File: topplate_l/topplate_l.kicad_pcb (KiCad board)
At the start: 2 copper layers, 133.3 x 104.8 mm, 28 parts, among them SW1 SW_PUSH, SW10 SW_PUSH, SW11 SW_PUSH, SW12 SW_PUSH, SW13 SW_PUSH, SW14 SW_PUSH, SW15 SW_PUSH, SW16 SW_PUSH, SW17 SW_PUSH, SW18 SW_PUSH, SW19 SW_PUSH, SW2 SW_PUSH, SW20 SW_PUSH, SW21 SW_PUSH, SW22 SW_PUSH, SW3 SW_PUSH, SW4 SW_PUSH, SW5 SW_PUSH, SW6 SW_PUSH, SW7 SW_PUSH, SW8 SW_PUSH, SW9 SW_PUSH

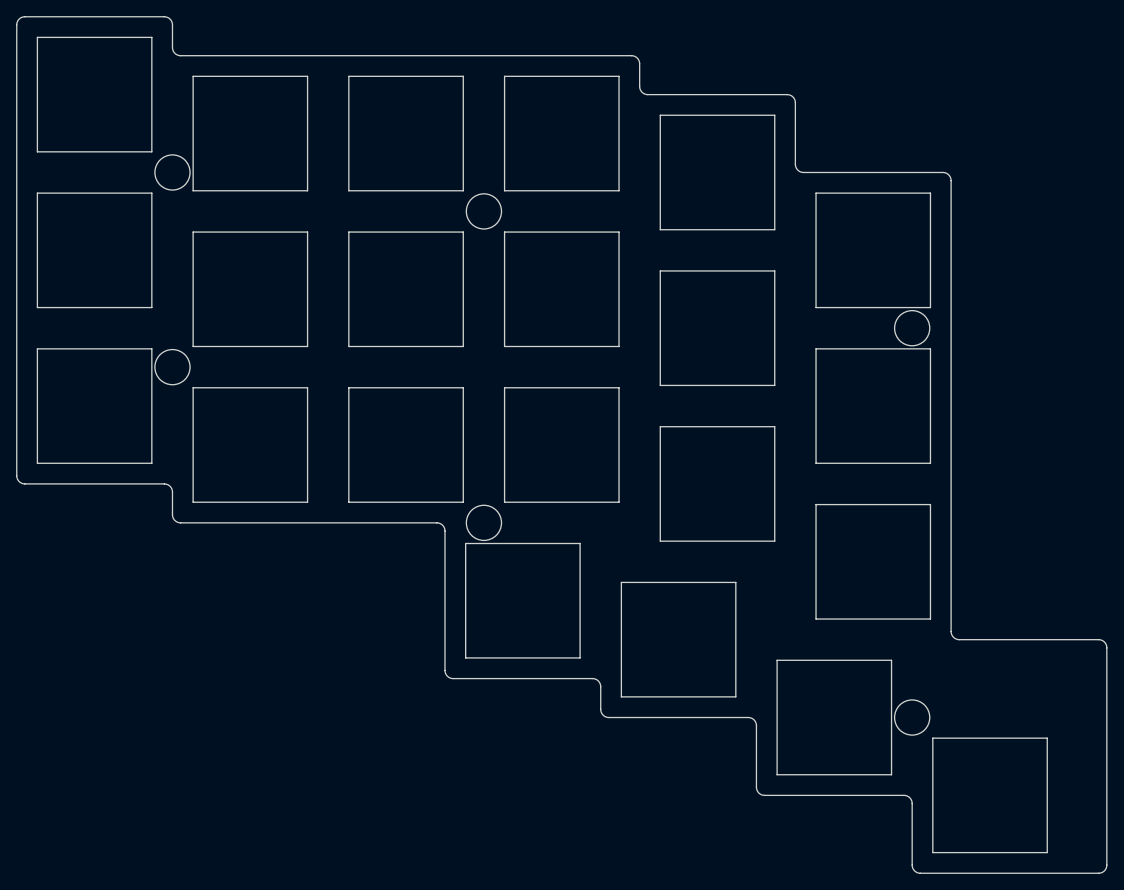
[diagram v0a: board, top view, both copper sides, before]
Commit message: added gnd mask
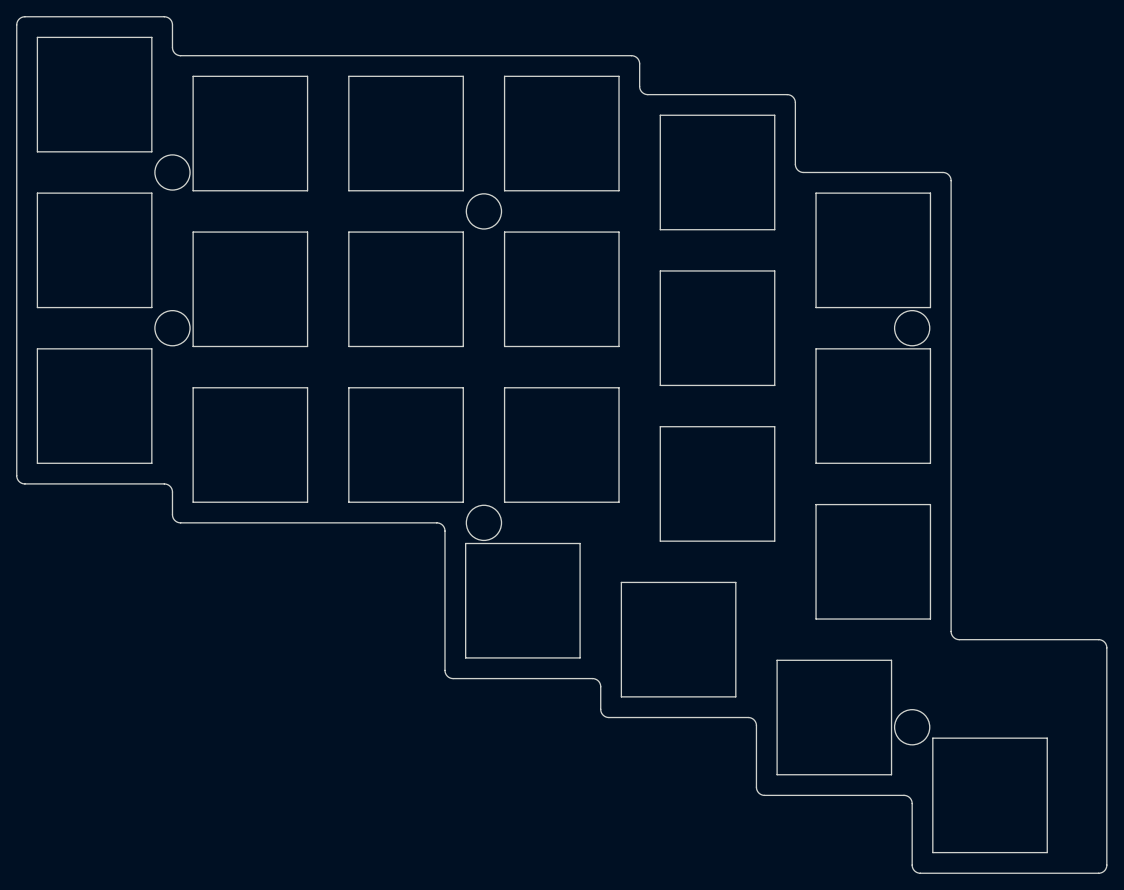
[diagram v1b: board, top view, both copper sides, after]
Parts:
- moved Ref** 4.76 mm to (38.1, 59.5)
- moved Ref** 1.19 mm to (128.6, 108.3)
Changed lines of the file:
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@@
   )
   (footprint "kbd:M2_HOLE_v2" (layer "F.Cu")
-    (at 38.1 64.29375)
+    (at 38.1 59.53125)
     (descr "Mounting Hole 2.2mm, no annular, M2")
     (tags "mounting hole 2.2mm no annular m2")
@@
   )
   (footprint "kbd:M2_HOLE_v2" (layer "F.Cu")
-    (at 128.5875 107.15625)
+    (at 128.5875 108.346875)
     (descr "Mounting Hole 2.2mm, no annular, M2")
     (tags "mounting hole 2.2mm no annular m2")

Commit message: fixed for order
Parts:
- Ref** (x6): footprint kbd:M2_HOLE_v2 -> kbd:M2_Hole_TH
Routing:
- added copper zone on F.Cu, net (none)
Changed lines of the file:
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@@
       (stroke (width 0.15) (type solid)) (layer "F.Fab"))
   )
-  (footprint "kbd:M2_HOLE_v2" (layer "F.Cu")
+  (footprint "kbd:M2_Hole_TH" (layer "F.Cu")
     (at 76.2 45.24375)
-    (descr "Mounting Hole 2.2mm, no annular, M2")
-    (tags "mounting hole 2.2mm no annular m2")
-    (attr exclude_from_pos_files exclude_from_bom)
-    (fp_text reference "Ref**" (at -0.95 -0.55) (layer "F.Fab") hide
-        (effects (font (size 1 1) (thickness 0.15)))
-    )
-    (fp_text value "Val**" (at 0 0.55) (layer "F.Fab") hide
-        (effects (font (size 1 1) (thickness 0.15)))
-    )
-    (pad "" np_thru_hole circle (at 0 0) (size 4.3 4.3) (drill 4.3) (layers "*.Cu" "*.Mask"))
-  )
-  (footprint "kbd:M2_HOLE_v2" (layer "F.Cu")
+    (attr through_hole)
+    (fp_text reference "Ref**" (at 0 0.5) (layer "F.SilkS")
+        (effects (font (size 1 1) (thickness 0.15)))
+    )
+    (fp_text value "Val**" (at 0 -0.5) (layer "F.Fab")
+        (effects (font (size 1 1) (thickness 0.15)))
+    )
+    (pad "" thru_hole circle (at 0 0) (size 4.2 4.2) (drill 2.3) (layers "*.Cu" "*.Mask"))
+  )
+  (footprint "kbd:M2_Hole_TH" (layer "F.Cu")
     (at 128.5875 59.53125)
-    (descr "Mounting Hole 2.2mm, no annular, M2")
-    (tags "mounting hole 2.2mm no annular m2")
-    (attr exclude_from_pos_files exclude_from_bom)
-    (fp_text reference "Ref**" (at -0.95 -0.55) (layer "F.Fab") hide
-        (effects (font (size 1 1) (thickness 0.15)))
-    )
-    (fp_text value "Val**" (at 0 0.55) (layer "F.Fab") hide
-        (effects (font (size 1 1) (thickness 0.15)))
-    )
-    (pad "" np_thru_hole circle (at 0 0) (size 4.3 4.3) (drill 4.3) (layers "*.Cu" "*.Mask"))
+    (attr through_hole)
+    (fp_text reference "Ref**" (at 0 0.5) (layer "F.SilkS")
+        (effects (font (size 1 1) (thickness 0.15)))
+    )
+    (fp_text value "Val**" (at 0 -0.5) (layer "F.Fab")
+        (effects (font (size 1 1) (thickness 0.15)))
+    )
+    (pad "" thru_hole circle (at 0 0) (size 4.2 4.2) (drill 2.3) (layers "*.Cu" "*.Mask"))
   )
   (footprint "kbd:SW_Hole" (layer "F.Cu")
@@
       (stroke (width 0.15) (type solid)) (layer "F.Fab"))
   )
-  (footprint "kbd:M2_HOLE_v2" (layer "F.Cu")
+  (footprint "kbd:M2_Hole_TH" (layer "F.Cu")
     (at 38.1 59.53125)
-    (descr "Mounting Hole 2.2mm, no annular, M2")
-    (tags "mounting hole 2.2mm no annular m2")
-    (attr exclude_from_pos_files exclude_from_bom)
-    (fp_text reference "Ref**" (at -0.95 -0.55) (layer "F.Fab") hide
-        (effects (font (size 1 1) (thickness 0.15)))
-    )
-    (fp_text value "Val**" (at 0 0.55) (layer "F.Fab") hide
-        (effects (font (size 1 1) (thickness 0.15)))
-    )
-    (pad "" np_thru_hole circle (at 0 0) (size 4.3 4.3) (drill 4.3) (layers "*.Cu" "*.Mask"))
+    (attr through_hole)
+    (fp_text reference "Ref**" (at 0 0.5) (layer "F.SilkS")
+        (effects (font (size 1 1) (thickness 0.15)))
+    )
+    (fp_text value "Val**" (at 0 -0.5) (layer "F.Fab")
+        (effects (font (size 1 1) (thickness 0.15)))
+    )
+    (pad "" thru_hole circle (at 0 0) (size 4.2 4.2) (drill 2.3) (layers "*.Cu" "*.Mask"))
   )
   (footprint "kbd:SW_Hole" (layer "F.Cu")
@@
       (stroke (width 0.15) (type solid)) (layer "F.Fab"))
   )
-  (footprint "kbd:M2_HOLE_v2" (layer "F.Cu")
+  (footprint "kbd:M2_Hole_TH" (layer "F.Cu")
     (at 38.1 40.48125)
-    (descr "Mounting Hole 2.2mm, no annular, M2")
-    (tags "mounting hole 2.2mm no annular m2")
-    (attr exclude_from_pos_files exclude_from_bom)
-    (fp_text reference "Ref**" (at -0.95 -0.55) (layer "F.Fab") hide
-        (effects (font (size 1 1) (thickness 0.15)))
-    )
-    (fp_text value "Val**" (at 0 0.55) (layer "F.Fab") hide
-        (effects (font (size 1 1) (thickness 0.15)))
-    )
-    (pad "" np_thru_hole circle (at 0 0) (size 4.3 4.3) (drill 4.3) (layers "*.Cu" "*.Mask"))
-  )
-  (footprint "kbd:M2_HOLE_v2" (layer "F.Cu")
+    (attr through_hole)
+    (fp_text reference "Ref**" (at 0 0.5) (layer "F.SilkS")
+        (effects (font (size 1 1) (thickness 0.15)))
+    )
+    (fp_text value "Val**" (at 0 -0.5) (layer "F.Fab")
+        (effects (font (size 1 1) (thickness 0.15)))
+    )
+    (pad "" thru_hole circle (at 0 0) (size 4.2 4.2) (drill 2.3) (layers "*.Cu" "*.Mask"))
+  )
+  (footprint "kbd:M2_Hole_TH" (layer "F.Cu")
     (at 128.5875 108.346875)
-    (descr "Mounting Hole 2.2mm, no annular, M2")
-    (tags "mounting hole 2.2mm no annular m2")
-    (attr exclude_from_pos_files exclude_from_bom)
-    (fp_text reference "Ref**" (at -0.95 -0.55) (layer "F.Fab") hide
-        (effects (font (size 1 1) (thickness 0.15)))
-    )
-    (fp_text value "Val**" (at 0 0.55) (layer "F.Fab") hide
-        (effects (font (size 1 1) (thickness 0.15)))
-    )
-    (pad "" np_thru_hole circle (at 0 0) (size 4.3 4.3) (drill 4.3) (layers "*.Cu" "*.Mask"))
+    (attr through_hole)
+    (fp_text reference "Ref**" (at 0 0.5) (layer "F.SilkS")
+        (effects (font (size 1 1) (thickness 0.15)))
+    )
+    (fp_text value "Val**" (at 0 -0.5) (layer "F.Fab")
+        (effects (font (size 1 1) (thickness 0.15)))
+    )
+    (pad "" thru_hole circle (at 0 0) (size 4.2 4.2) (drill 2.3) (layers "*.Cu" "*.Mask"))
   )
   (footprint "kbd:SW_Hole" (layer "F.Cu")
@@
       (stroke (width 0.15) (type solid)) (layer "F.Fab"))
   )
-  (footprint "kbd:M2_HOLE_v2" (layer "F.Cu")
+  (footprint "kbd:M2_Hole_TH" (layer "F.Cu")
     (at 76.2 83.34375)
-    (descr "Mounting Hole 2.2mm, no annular, M2")
-    (tags "mounting hole 2.2mm no annular m2")
-    (attr exclude_from_pos_files exclude_from_bom)
-    (fp_text reference "Ref**" (at -0.95 -0.55) (layer "F.Fab") hide
-        (effects (font (size 1 1) (thickness 0.15)))
-    )
-    (fp_text value "Val**" (at 0 0.55) (layer "F.Fab") hide
-        (effects (font (size 1 1) (thickness 0.15)))
-    )
-    (pad "" np_thru_hole circle (at 0 0) (size 4.3 4.3) (drill 4.3) (layers "*.Cu" "*.Mask"))
+    (attr through_hole)
+    (fp_text reference "Ref**" (at 0 0.5) (layer "F.SilkS")
+        (effects (font (size 1 1) (thickness 0.15)))
+    )
+    (fp_text value "Val**" (at 0 -0.5) (layer "F.Fab")
+        (effects (font (size 1 1) (thickness 0.15)))
+    )
+    (pad "" thru_hole circle (at 0 0) (size 4.2 4.2) (drill 2.3) (layers "*.Cu" "*.Mask"))
   )
   (footprint "kbd:SW_Hole" (layer "F.Cu")
@@
   (gr_arc (start 132.35 40.48125) (mid 133.057107 40.774143) (end 133.35 41.48125)
     (stroke (width 0.1) (type default)) (layer "Edge.Cuts"))
+  (zone (net 0) (net_name "") (layer "F.Cu") (hatch edge 0.5)
+    (connect_pads (clearance 1))
+    (min_thickness 0.25) (filled_areas_thickness no)
+    (fill yes (thermal_gap 0.5) (thermal_bridge_width 0.5) (island_removal_mode 1) (island_area_min 10))
+    (polygon
+      (pts
+        (xy 133.35 40.48125)
+        (xy 114.3 40.48125)
+        (xy 114.3 30.95625)
+        (xy 95.25 30.95625)
+        (xy 95.25 26.19375)
+        (xy 38.1 26.19375)
+        (xy 38.1 21.43125)
+        (xy 19.05 21.43125)
+        (xy 19.05 78.58125)
+        (xy 38.1 78.58125)
+        (xy 38.1 83.34375)
+        (xy 71.4375 83.34375)
+        (xy 71.4375 102.39375)
+        (xy 90.4875 102.39375)
+        (xy 90.4875 107.15625)
+        (xy 109.5375 107.15625)
+        (xy 109.5375 116.68125)
+        (xy 128.5875 116.68125)
+        (xy 128.5875 126.20625)
+        (xy 152.4 126.20625)
+        (xy 152.4 97.63125)
+        (xy 133.35 97.63125)
+      )
+    )
+  )
   (group "" (id b9ec9487-7741-4b36-bab2-a6f5571cd5b5)
     (members

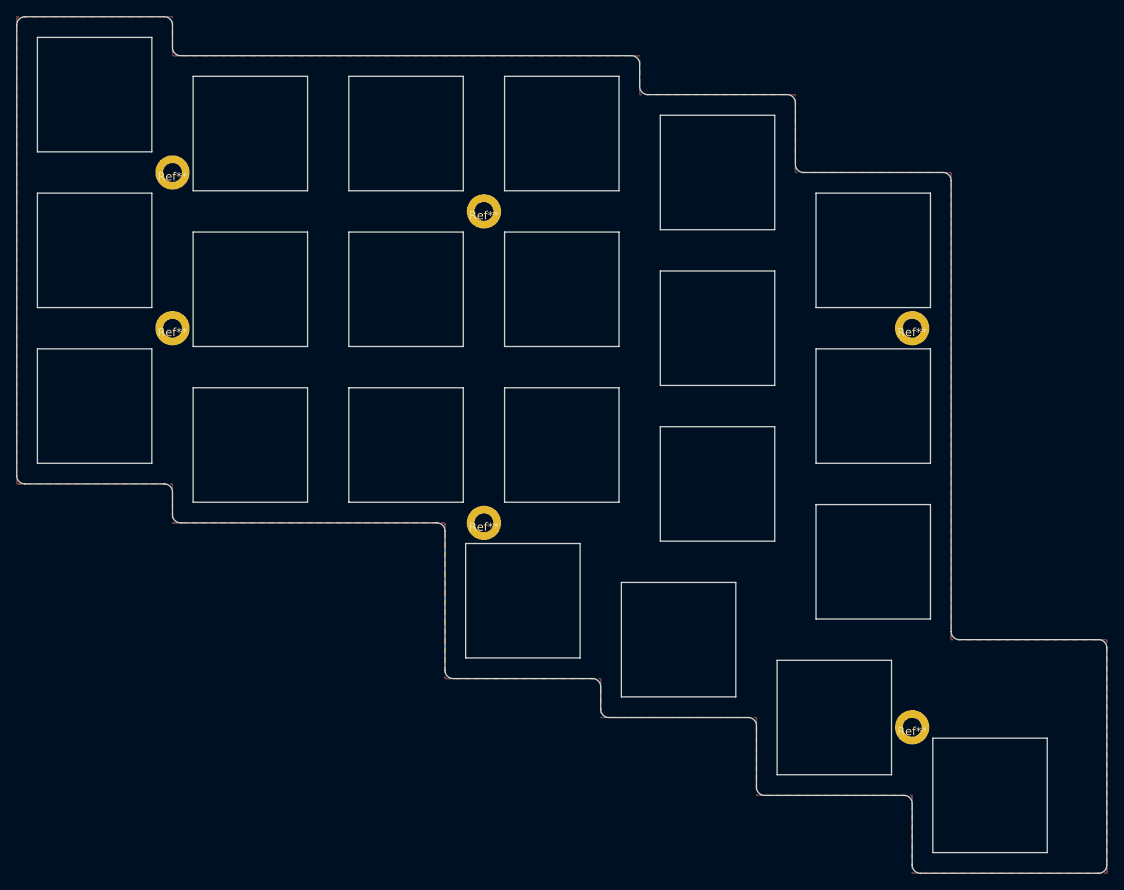
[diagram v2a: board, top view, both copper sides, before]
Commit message: fixed #6
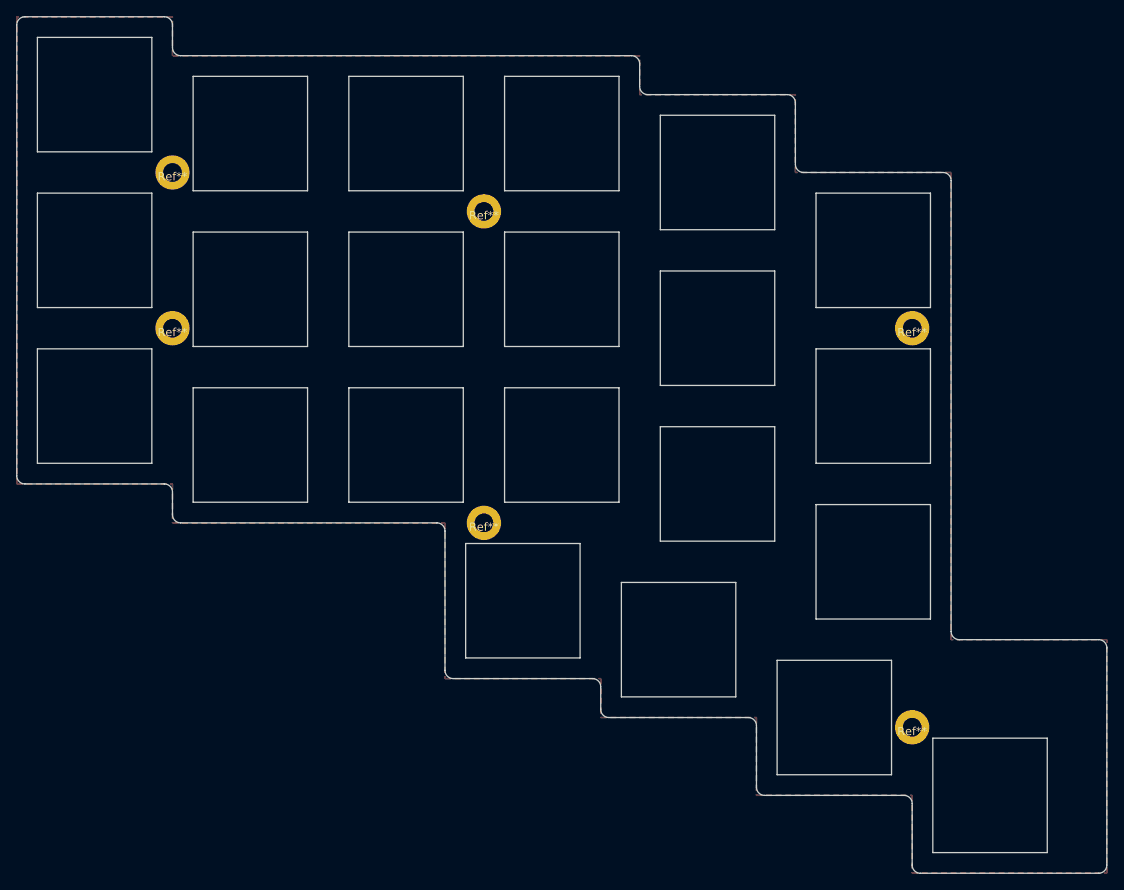
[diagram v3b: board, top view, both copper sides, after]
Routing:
- added copper zone on B.Cu, net (none)
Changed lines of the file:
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@@
   (gr_arc (start 132.35 40.48125) (mid 133.057107 40.774143) (end 133.35 41.48125)
     (stroke (width 0.1) (type default)) (layer "Edge.Cuts"))
-  (zone (net 0) (net_name "") (layer "F.Cu") (hatch edge 0.5)
+  (zone (net 0) (net_name "") (layers "F&B.Cu") (hatch edge 0.5)
     (connect_pads (clearance 1))
     (min_thickness 0.25) (filled_areas_thickness no)
